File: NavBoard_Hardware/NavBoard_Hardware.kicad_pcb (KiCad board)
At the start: 2 copper layers, 124.5 x 79.2 mm, 41 parts, among them J1 Conn_01x06_Male, U1 OKI-5V, U2 BHI160B, U3 ICM-20608-G, U4 OKI-3V3, U6 Raspberry_Pi

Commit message: CDR Changes 2
Ready to release, signatures to be added
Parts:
- added G***: LOGO, MRDT_Silkscreens:0_MRDT_Logo_60mm, B.Cu at (92.2, 79.0)
- moved J1 9.91 mm to (48.0, 87.4)
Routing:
- net M8Q-TX: track 101.4 -> 111.3 mm
- net M8Q-RX: track 94.3 -> 104.2 mm
- net I2C-SDA: track 108.3 -> 118.2 mm
- net I2C-SCL: track 107.1 -> 117.0 mm
- net +5V: track 108.1 -> 118.0 mm
- net GND: track 93.1 -> 84.8 mm, vias 11 -> 10
- net Net-(C12-Pad1): track 3.25 -> 4.16 mm
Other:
- board text added: "+"
- board text added: "-"
- board text added: "Navigation Board, Rev 1.1 Mars Rover Design Team Missouri S&T, 2022 Malacki Ehlers and Jorge Noriega"
- board text added: "RX"
- board text added: "SCL"
- board text added: "SDA"
- board text added: "TX"

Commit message: Signature
Added my signature on the board. Still needs one more.
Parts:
- added G***: LOGO, MRDT_Silkscreens:z_sig_Jorge_Noriega_34.3mmx15.1mm, F.Cu at (138.5, 104.0)

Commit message: Fixed Signature
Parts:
- removed the G*** at (138.5, 104.0)
- added G***: LOGO, Signature:z_sig_Jorge_Noriega_34.3mmx15.1mm, F.Cu at (145.8, 103.0)

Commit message: Added signature
Final updates, ready to order
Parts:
- removed the G*** at (145.8, 103.0)
- added G***: LOGO, Signatures:z_sig_Jorge_Noriega_34.3mmx15.1mm, F.Cu at (142.2, 57.4)
- added G***: LOGO, Signatures:z_sig_Malacki_Ehlers_15.3mmx4.7mm, F.Cu at (142.0, 74.9)

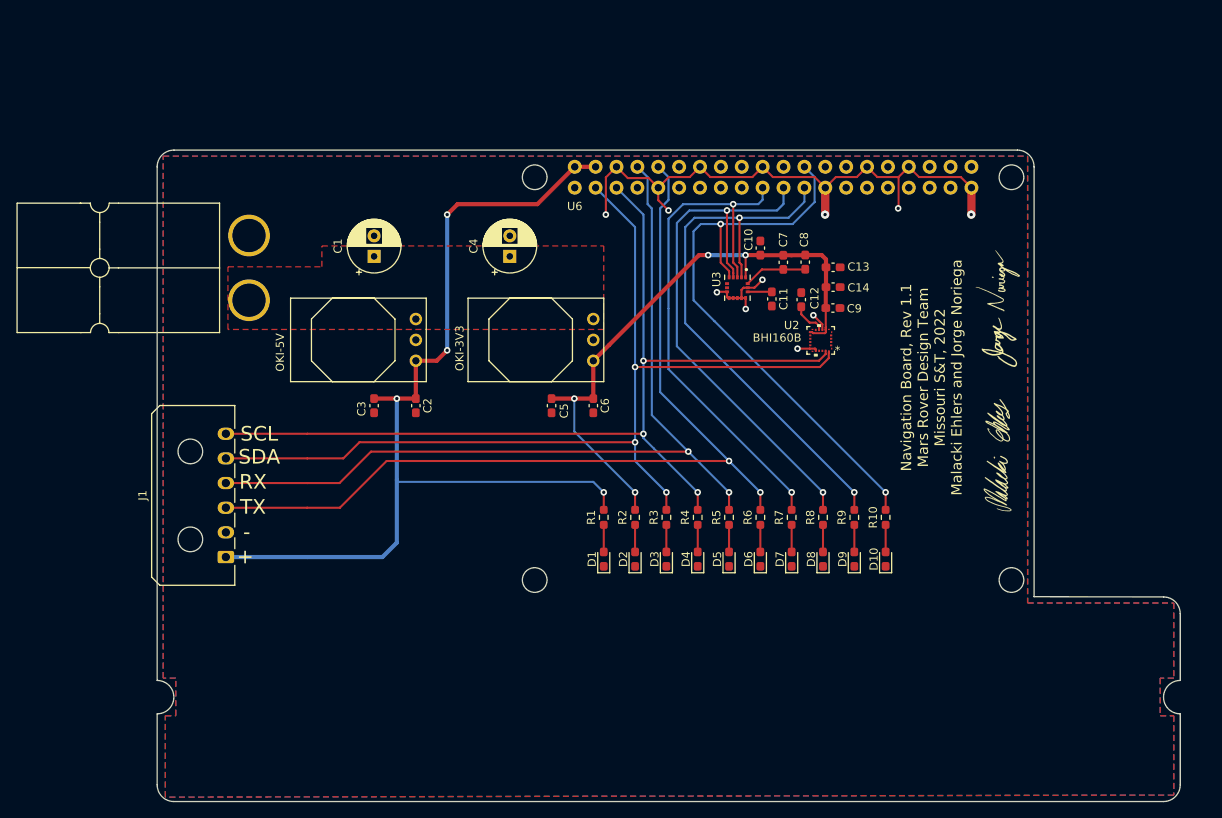
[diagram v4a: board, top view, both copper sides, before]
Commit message: Initial pass at stackable arrangement
Attempting to replace previous board design with 2 daughter boards, using a Teensy 4.1 instead of a Raspberry Pi
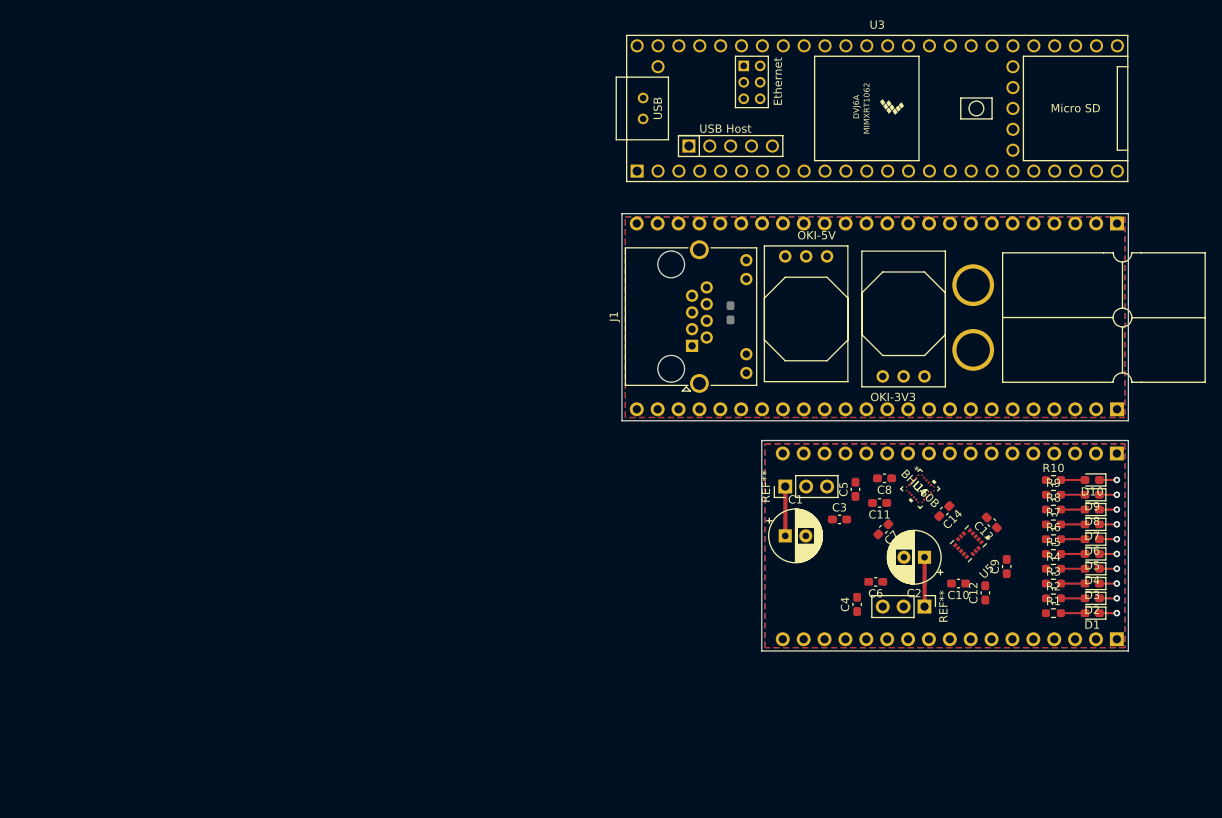
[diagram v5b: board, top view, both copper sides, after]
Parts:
- removed G***: LOGO, Signatures:z_sig_Jorge_Noriega_34.3mmx15.1mm
- removed G***: LOGO, Signatures:z_sig_Malacki_Ehlers_15.3mmx4.7mm
- removed G***: LOGO, MRDT_Silkscreens:0_MRDT_Logo_60mm
- removed U6: Raspberry_Pi, MRDT_Shields:RaspberryPi_THT_BOTTOM
- added C15: 0.1uF, Capacitor_SMD:C_0603_1608Metric_Pad1.08x0.95mm_HandSolder, B.Cu at (109.4, 57.7)
- added REF**: PinHeader_1x03_P2.54mm_Vertical, Connector_PinHeader_2.54mm:PinHeader_1x03_P2.54mm_Vertical, F.Cu at (133.0, 93.4)
- added REF**: PinHeader_1x03_P2.54mm_Vertical, Connector_PinHeader_2.54mm:PinHeader_1x03_P2.54mm_Vertical, F.Cu at (116.1, 78.8)
- added REF**: PinHeader_1x17_P2.54mm_Vertical, Connector_PinHeader_2.54mm:PinHeader_1x17_P2.54mm_Vertical, B.Cu at (156.4, 74.8)
- added REF**: PinSocket_1x24_P2.54mm_Vertical, Connector_PinSocket_2.54mm:PinSocket_1x24_P2.54mm_Vertical, B.Cu at (156.4, 69.4)
- added REF**: PinHeader_1x17_P2.54mm_Vertical, Connector_PinHeader_2.54mm:PinHeader_1x17_P2.54mm_Vertical, B.Cu at (156.4, 97.4)
- added REF**: PinSocket_1x24_P2.54mm_Vertical, Connector_PinSocket_2.54mm:PinSocket_1x24_P2.54mm_Vertical, B.Cu at (156.4, 46.8)
- added U5: ICM-20608-G, ICM-20608-G:ICM-20608-G, F.Cu at (138.3, 85.8)
- C10: value 10nF -> 0.47uF
- C12: value 0.47uF -> 2.2uF
- C13: value 1uF -> 10nF
- C2: value 10uF -> 22uF 50V; footprint Capacitor_SMD:C_0603_1608Metric_Pad1.08x0.95mm_HandSolder -> Capacitor_THT:CP_Radial_D6.3mm_P2.50mm
- C3: value 0.1uF -> 10uF
- C4: value 22uF 50V -> 10uF; footprint Capacitor_THT:CP_Radial_D6.3mm_P2.50mm -> Capacitor_SMD:C_0603_1608Metric_Pad1.08x0.95mm_HandSolder
- C5: value 10uF -> 0.1uF
- C7: value 0.1uF -> 1uF
- C8: value 2.2uF -> 0.1uF
- J1: value Conn_01x06_Male -> 8P8C_LED_Shielded; footprint Connector_Molex:Molex_Micro-Fit_3.0_43650-0600_1x06_P3.00mm_Horizontal -> Connector_RJ:RJ45_Amphenol_RJHSE538X
- U2: value BHI160B -> OKI-3V3; footprint BHI160B:BHI160B -> MRDT_Devices:OKI_Horizontal
- U3: value ICM-20608-G -> Teensy4.1; footprint ICM-20608-G:ICM-20608-G -> teensy:Teensy41
- U4: value OKI-3V3 -> BHI160B; footprint MRDT_Devices:OKI_Horizontal -> BHI160B:BHI160B
- moved Conn1 89.2 mm to (138.9, 62.2), turned to 180 degrees
- moved C2 64.6 mm to (133.0, 87.4), turned to 180 degrees
- moved J1 62.3 mm to (104.7, 61.7)
- moved C1 60.5 mm to (116.1, 84.8), turned to 0 degrees
- moved C4 59.8 mm to (124.8, 93.1)
- moved D1 59.8 mm to (153.4, 94.2), turned to 180 degrees
- moved C3 58.3 mm to (122.7, 82.8), turned to 0 degrees
- moved R1 55.9 mm to (148.7, 94.2), turned to 0 degrees
- moved D2 55.8 mm to (153.4, 92.4), turned to 180 degrees
- moved D3 51.9 mm to (153.4, 90.6), turned to 180 degrees
- moved R2 51.8 mm to (148.7, 92.4), turned to 0 degrees
- moved D4 48.0 mm to (153.4, 88.8), turned to 180 degrees
- moved R3 47.8 mm to (148.7, 90.6), turned to 0 degrees
- moved C10 47.4 mm to (137.1, 90.6), turned to 180 degrees
- moved U1 45.6 mm to (116.1, 50.8), turned to 0 degrees
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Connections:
- C10 pad 1: +3V3 -> Net-(C10-Pad1)
- C12 pad 1: Net-(C12-Pad1) -> +3V3
- C12 pad 2: GND -> Net-(C12-Pad2)
- C14 pad 1: +3V3 -> GND
- C14 pad 2: GND -> +3V3
- C2 pad 1: +5V -> +12V
- C4 pad 1: +12V -> +3V3
- C5 pad 1: +3V3 -> +5V
- C7 pad 2: Net-(C7-Pad2) -> GND
- C8 pad 2: Net-(C7-Pad2) -> GND
- C9 pad 1: GND -> +3V3
- C9 pad 2: +3V3 -> Net-(C12-Pad2)
- J1 pad 1: +5V -> /ETHERNET_TX+
- J1 pad 2: GND -> Net-(C15-Pad1)
- J1 pad 3: M8Q-TX -> /ETHERNET_TX-
- J1 pad 4: M8Q-RX -> /ETHERNET_RX+
- J1 pad 5: I2C-SDA -> Net-(C15-Pad1)
- J1 pad 6: I2C-SCL -> /ETHERNET_RX-
- R10 pad 1: ICM-CS -> unconnected-(R10-Pad1)
- R3 pad 1: I2C-SDA -> unconnected-(R3-Pad1)
- R4 pad 1: I2C-SCL -> unconnected-(R4-Pad1)
- R5 pad 1: M8Q-RX -> unconnected-(R5-Pad1)
- R6 pad 1: M8Q-TX -> unconnected-(R6-Pad1)
- R7 pad 1: ICM-SDI -> unconnected-(R7-Pad1)
- R8 pad 1: ICM-SDO -> unconnected-(R8-Pad1)
- R9 pad 1: ICM-SCLK -> unconnected-(R9-Pad1)
- U2 pad 1: Net-(U2-Pad1) -> +12V
- U2 pad 2: Net-(U2-Pad2) -> GND
- U2 pad 3: Net-(U2-Pad3) -> +3V3
- U3 pad 1: +3V3 -> GND
- U3 pad 10: GND -> unconnected-(U3-Pad10)
- U3 pad 11: GND -> unconnected-(U3-Pad11)
- U3 pad 12: GND -> unconnected-(U3-Pad12)
- U3 pad 13: GND -> /ICM_SDI
- U3 pad 14: Net-(C11-Pad1) -> /ICM_SDO
- U3 pad 15: GND -> unconnected-(U3-Pad15)
- U3 pad 16: Net-(C7-Pad2) -> unconnected-(U3-Pad16)
- U3 pad 2: ICM-SCLK -> unconnected-(U3-Pad2)
- U3 pad 3: ICM-SDI -> unconnected-(U3-Pad3)
- U3 pad 4: ICM-SDO -> unconnected-(U3-Pad4)
- U3 pad 5: ICM-CS -> unconnected-(U3-Pad5)
- U3 pad 6: Net-(U3-Pad6) -> unconnected-(U3-Pad6)
- U3 pad 7: (no net) -> unconnected-(U3-Pad7)
- U3 pad 8: GND -> unconnected-(U3-Pad8)
- U3 pad 9: GND -> unconnected-(U3-Pad9)
- U4 pad 1: +12V -> unconnected-(U4-Pad1)
- U4 pad 2: GND -> unconnected-(U4-Pad2)
- U4 pad 3: +3V3 -> unconnected-(U4-Pad3)
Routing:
- net I2C-SDA: track 118.2 -> 0.00 mm, vias 3 -> 0
- net +5V: track 118.0 -> 0.00 mm, vias 4 -> 0
- net I2C-SCL: track 117.0 -> 0.00 mm, vias 3 -> 0
- net M8Q-TX: track 111.3 -> 0.00 mm, vias 2 -> 0
- net M8Q-RX: track 104.2 -> 0.00 mm, vias 2 -> 0
- net +3V3: track 74.2 -> 0.00 mm, vias 4 -> 0
- net ICM-CS: track 71.5 -> 0.00 mm, vias 2 -> 0
- net ICM-SCLK: track 67.8 -> 0.00 mm, vias 2 -> 0
- net ICM-SDO: track 66.6 -> 0.00 mm, vias 2 -> 0
- net ICM-SDI: track 64.6 -> 0.00 mm, vias 2 -> 0
- net GND: track 84.8 -> 21.3 mm
- net +12V: track 0.00 -> 12.0 mm
- net Net-(C7-Pad2): track 7.68 -> 0.00 mm
- net Net-(C12-Pad1): track 4.16 -> 0.00 mm
- net Net-(C11-Pad1): track 2.93 -> 0.00 mm
- added copper zone on In1.Cu, net GND
- removed copper zone on F.Cu, net +12V
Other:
- board size 124.5 x 79.2 mm -> 61.6 x 53.2 mm
- copper layers 2 -> 4
- net class Default removed
- board text removed: "+"
- board text removed: "-"
- board text removed: "Navigation Board, Rev 1.1 Mars Rover Design Team Missouri S&T, 2022 Malacki Ehlers and Jorge Noriega"
- board text removed: "RX"
- board text removed: "SCL"
- board text removed: "SDA"
- board text removed: "TX"

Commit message: Redesigned layoput
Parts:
- removed D10, D6, D7, D8, D9: BLUE, LED_SMD:LED_0603_1608Metric_Pad1.05x0.95mm_HandSolder
- removed REF** (x2): PinHeader_1x03_P2.54mm_Vertical, Connector_PinHeader_2.54mm:PinHeader_1x03_P2.54mm_Vertical
- removed REF** (x2): PinHeader_1x17_P2.54mm_Vertical, Connector_PinHeader_2.54mm:PinHeader_1x17_P2.54mm_Vertical
- removed REF** (x2): PinSocket_1x24_P2.54mm_Vertical, Connector_PinSocket_2.54mm:PinSocket_1x24_P2.54mm_Vertical
- added J10: Conn_01x16, Connector_PinSocket_2.54mm:PinSocket_1x16_P2.54mm_Vertical, B.Cu at (197.2, 88.1)
- added J11: Conn_01x16, Connector_PinSocket_2.54mm:PinSocket_1x16_P2.54mm_Vertical, B.Cu at (197.2, 67.8)
- added J12: Conn_01x24, Connector_PinHeader_2.54mm:PinHeader_1x24_P2.54mm_Vertical, B.Cu at (138.8, 65.3)
- added J13: Conn_01x16, Connector_PinSocket_2.54mm:PinSocket_1x16_P2.54mm_Vertical, B.Cu at (263.8, 88.2)
- added J14: Conn_01x16, Connector_PinSocket_2.54mm:PinSocket_1x16_P2.54mm_Vertical, B.Cu at (263.8, 67.9)
- added J15: Conn_01x03, Connector_PinSocket_2.54mm:PinSocket_1x03_P2.54mm_Vertical, B.Cu at (230.7, 85.1)
- added J16: Conn_01x03, Connector_PinSocket_2.54mm:PinSocket_1x03_P2.54mm_Vertical, B.Cu at (236.3, 71.1)
- added J2: 6 Pin Molex Micro-Fit, Connector_Molex:Molex_Micro-Fit_3.0_43650-0600_1x06_P3.00mm_Horizontal, F.Cu at (222.1, 85.6)
- added J3: Conn_01x24, Connector_PinSocket_2.54mm:PinSocket_1x24_P2.54mm_Vertical, F.Cu at (56.7, 90.7)
- added J4: Conn_01x24, Connector_PinSocket_2.54mm:PinSocket_1x24_P2.54mm_Vertical, B.Cu at (56.7, 85.7)
- added J6: Conn_01x24, Connector_PinSocket_2.54mm:PinSocket_1x24_P2.54mm_Vertical, B.Cu at (56.7, 70.4)
- added J7: Conn_01x24, Connector_PinSocket_2.54mm:PinSocket_1x24_P2.54mm_Vertical, F.Cu at (56.7, 65.3)
- added J8: Conn_01x06, Connector_PinSocket_2.00mm:PinSocket_2x03_P2.00mm_Vertical, B.Cu at (153.8, 76.8)
- added J9: Conn_01x24, Connector_PinHeader_2.54mm:PinHeader_1x24_P2.54mm_Vertical, B.Cu at (197.3, 90.7)
- added JP1: Solder Jumper, Jumper:SolderJumper-2_P1.3mm_Open_RoundedPad1.0x1.5mm, F.Cu at (245.6, 101.1)
- added R11: 4.7k, Resistor_SMD:R_0603_1608Metric_Pad0.98x0.95mm_HandSolder, F.Cu at (207.7, 95.7)
- added R12: 100, Resistor_SMD:R_0603_1608Metric_Pad0.98x0.95mm_HandSolder, F.Cu at (193.1, 44.3)
- added R13: 100, Resistor_SMD:R_0603_1608Metric_Pad0.98x0.95mm_HandSolder, F.Cu at (59.2, 52.2)
- added R14: 100, Resistor_SMD:R_0603_1608Metric_Pad0.98x0.95mm_HandSolder, F.Cu at (63.6, 52.2)
- added TP1: TestPoint, TestPoint:TestPoint_Pad_D2.0mm, F.Cu at (187.2, 36.4)
- added TP2: TestPoint, TestPoint:TestPoint_Pad_D2.0mm, F.Cu at (192.5, 31.4)
- added TP3: TestPoint, TestPoint:TestPoint_Pad_D2.0mm, F.Cu at (206.7, 103.5)
- added TP4: TestPoint, TestPoint:TestPoint_Pad_D2.0mm, F.Cu at (211.0, 99.0)
- C1: value 22uF 50V -> 0.1uF; footprint Capacitor_THT:CP_Radial_D6.3mm_P2.50mm -> Capacitor_SMD:C_0603_1608Metric_Pad1.08x0.95mm_HandSolder
- C10: value 0.47uF -> 10uF
- C11: value 0.47uF -> 0.1uF
- C13: value 10nF -> 0.1uF
- C14: value 0.1uF -> 0.47uF
- C15: value 0.1uF -> 10nF; moved to F.Cu
- C2: value 22uF 50V -> 1uF; footprint Capacitor_THT:CP_Radial_D6.3mm_P2.50mm -> Capacitor_SMD:C_0603_1608Metric_Pad1.08x0.95mm_HandSolder
- C3, C4: value 10uF -> 0.1uF
- C5: value 0.1uF -> 0.47uF; footprint Capacitor_SMD:C_0603_1608Metric_Pad1.08x0.95mm_HandSolder -> Capacitor_THT:CP_Radial_D6.3mm_P2.50mm
- C6, C9: value 0.1uF -> 22uF 50V
- C7: value 1uF -> 10uF
- C8: footprint Capacitor_SMD:C_0603_1608Metric_Pad1.08x0.95mm_HandSolder -> Capacitor_THT:CP_Radial_D6.3mm_P2.50mm
- R1: value 100 -> 43
- R10, R3, R4, R5, R6, R7, R8, R9: value 100 -> 4.7k
- R2: value 43 -> 100
- U1: value OKI-5V -> BHI160B; footprint MRDT_Devices:OKI_Horizontal -> BHI160B:BHI160B
- U2: value OKI-3V3 -> OKI-5V
- U3: value Teensy4.1 -> OKI-3V3; footprint teensy:Teensy41 -> MRDT_Devices:OKI_Horizontal
- U4: value BHI160B -> ICM-20608-G; footprint BHI160B:BHI160B -> ICM-20608-G:ICM-20608-G
- U5: value ICM-20608-G -> Teensy4.1; footprint ICM-20608-G:ICM-20608-G -> teensy:Teensy41
- moved C15 161.2 mm to (260.0, 115.2), turned to 0 degrees
- moved C6 141.5 mm to (255.3, 30.6), turned to 0 degrees
- moved C5 136.1 mm to (260.5, 72.3), turned to -90 degrees
- moved C8 132.4 mm to (260.5, 81.4), turned to -90 degrees
- moved C9 128.2 mm to (268.0, 60.0), turned to 0 degrees
- moved C7 119.3 mm to (244.0, 56.1), turned to 0 degrees
- moved R4 118.3 mm to (264.4, 113.5)
- moved U1 117.6 mm to (231.0, 75.8)
- moved D2 108.5 mm to (260.0, 112.6), turned to 0 degrees
- moved R2 105.7 mm to (249.4, 124.5)
- moved U4 105.7 mm to (238.1, 79.6), turned to 0 degrees
- moved R3 102.2 mm to (245.0, 124.5)
- moved D4 101.9 mm to (59.3, 49.6), turned to 0 degrees
- moved D5 97.2 mm to (63.7, 49.6), turned to 0 degrees
- moved R1 96.9 mm to (240.7, 124.5)
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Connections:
- C1 pad 1: +12V -> Net-(C1-Pad1)
- C1 pad 2: GND -> Net-(C1-Pad2)
- C10 pad 1: Net-(C10-Pad1) -> +3V3
- C11 pad 1: Net-(C11-Pad1) -> +3V3
- C12 pad 2: Net-(C12-Pad2) -> GND
- C14 pad 1: GND -> +3V3
- C14 pad 2: +3V3 -> GND
- C15 pad 1: Net-(C15-Pad1) -> +3V3
- C15 pad 2: Net-(C15-Pad2) -> GND
- C2 pad 1: +12V -> +3V3
- C3 pad 1: +5V -> +3V3
- C5 pad 1: +5V -> +3V3
- C6 pad 1: +3V3 -> /OKI - 3V3/+12V
- C7 pad 1: +3V3 -> +5V
- C8 pad 1: +3V3 -> +5V
- C9 pad 1: +3V3 -> /OKI - 3V3/+12V
- C9 pad 2: Net-(C12-Pad2) -> GND
- Conn1 pad 2: +12V -> /OKI - 3V3/+12V
- D3 pad 1: GND -> /teensy_4.1/UART_Status_LED
- D4 pad 1: GND -> /teensy_4.1/SPI_Status_LED
- D5 pad 1: GND -> /teensy_4.1/I2C_Status_LED
- J1 pad 1: /ETHERNET_TX+ -> /Main Board/ETHERNET_TX+
- J1 pad 10: /ETHERNET_LED -> /Main Board/ETHERNET_LED
- J1 pad 2: Net-(C15-Pad1) -> Net-(C1-Pad1)
- J1 pad 3: /ETHERNET_TX- -> /Main Board/ETHERNET_TX-
- J1 pad 4: /ETHERNET_RX+ -> /Main Board/ETHERNET_RX+
- J1 pad 5: Net-(C15-Pad1) -> Net-(C1-Pad1)
- J1 pad 6: /ETHERNET_RX- -> /Main Board/ETHERNET_RX-
- J1 pad 8: Net-(C15-Pad2) -> Net-(C1-Pad2)
- R1 pad 1: +5V -> +3V3
- R10 pad 1: unconnected-(R10-Pad1) -> Net-(R10-Pad1)
- R10 pad 2: Net-(D10-Pad2) -> GND
- R2 pad 1: +3V3 -> +5V
- R3 pad 1: unconnected-(R3-Pad1) -> /I2C-SDA
- R3 pad 2: Net-(D3-Pad2) -> GND
- R4 pad 1: unconnected-(R4-Pad1) -> /I2C-SCL
- R4 pad 2: Net-(D4-Pad2) -> GND
- R5 pad 1: unconnected-(R5-Pad1) -> Net-(R5-Pad1)
- R5 pad 2: Net-(D5-Pad2) -> GND
- R6 pad 1: unconnected-(R6-Pad1) -> Net-(R6-Pad1)
- R6 pad 2: Net-(D6-Pad2) -> GND
- R7 pad 1: unconnected-(R7-Pad1) -> Net-(R7-Pad1)
- R7 pad 2: Net-(D7-Pad2) -> GND
- R8 pad 1: unconnected-(R8-Pad1) -> Net-(R8-Pad1)
- R8 pad 2: Net-(D8-Pad2) -> GND
- R9 pad 1: unconnected-(R9-Pad1) -> Net-(R9-Pad1)
- R9 pad 2: Net-(D9-Pad2) -> GND
- U1 pad 1: +12V -> (no net)
- U1 pad 2: GND -> (no net)
- U1 pad 3: +5V -> Net-(R8-Pad1)
- U2 pad 1: +12V -> /OKI - 3V3/+12V
- U2 pad 3: +3V3 -> +5V
- U3 pad 1: GND -> /OKI - 3V3/+12V
- U3 pad 2: unconnected-(U3-Pad2) -> GND
- U3 pad 3: unconnected-(U3-Pad3) -> +3V3
- U4 pad 1: unconnected-(U4-Pad1) -> +3V3
- U4 pad 10: Net-(C11-Pad1) -> unconnected-(U4-Pad10)
- U4 pad 13: +3V3 -> GND
- U4 pad 14: unconnected-(U4-Pad14) -> +3V3
- U4 pad 15: unconnected-(U4-Pad15) -> GND
- U4 pad 16: unconnected-(U4-Pad16) -> +3V3
- U4 pad 2: unconnected-(U4-Pad2) -> /SPI-SCLK
- U4 pad 3: unconnected-(U4-Pad3) -> /SPI-MOSI
- U4 pad 4: unconnected-(U4-Pad4) -> /SPI-MISO
- U4 pad 5: unconnected-(U4-Pad5) -> /SPI-CS
- U4 pad 6: unconnected-(U4-Pad6) -> Net-(R11-Pad1)
- U4 pad 7: unconnected-(U4-Pad7) -> (no net)
- U4 pad 8: +3V3 -> Net-(R10-Pad1)
- U4 pad 9: GND -> unconnected-(U4-Pad9)
- U5 pad 1: +3V3 -> GND
- U5 pad 10: GND -> /Teensy Shield/Pin8
- U5 pad 11: GND -> /Teensy Shield/Pin9
- U5 pad 12: GND -> /Teensy Shield/Pin10
- U5 pad 13: GND -> /Teensy Shield/Pin11
- U5 pad 14: Net-(C10-Pad1) -> /Teensy Shield/Pin12
- U5 pad 15: GND -> +3V3
- U5 pad 16: Net-(C12-Pad2) -> /Teensy Shield/Pin24
- U5 pad 2: /ICM_SCL -> /Teensy Shield/Pin0
- U5 pad 3: /ICM_SDI -> /Teensy Shield/Pin1
- U5 pad 4: /ICM_SDO -> /Teensy Shield/Pin2
- U5 pad 5: unconnected-(U5-Pad5) -> /Teensy Shield/Pin3
- U5 pad 6: unconnected-(U5-Pad6) -> /Teensy Shield/Pin4
- U5 pad 7: (no net) -> /Teensy Shield/Pin5
- U5 pad 8: GND -> /Teensy Shield/Pin6
- U5 pad 9: GND -> /Teensy Shield/Pin7
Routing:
- net +12V: track 12.0 -> 0.00 mm
- net GND: track 21.3 -> 15.2 mm, vias 10 -> 0
- net /Teensy Shield/Pin41: track 0.00 -> 5.08 mm
- net /Teensy Shield/Pin38: track 0.00 -> 5.08 mm
- net /Teensy Shield/Pin36: track 0.00 -> 5.08 mm
- net /Teensy Shield/Pin22: track 0.00 -> 5.08 mm
- net /Teensy Shield/Pin20: track 0.00 -> 5.08 mm
- net /Teensy Shield/Pin40: track 0.00 -> 5.08 mm
- net /Teensy Shield/Pin34: track 0.00 -> 5.08 mm
- net /Teensy Shield/Pin17: track 0.00 -> 5.08 mm
- net /Teensy Shield/Pin15: track 0.00 -> 5.08 mm
- net /Teensy Shield/Pin13: track 0.00 -> 5.08 mm
- net /Teensy Shield/Pin3V3_Right: track 0.00 -> 5.08 mm
- net +5V: track 0.00 -> 5.08 mm
- net /Teensy Shield/Pin39: track 0.00 -> 5.08 mm
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- removed copper zone on B.Cu, net GND
- removed copper zone on F.Cu, net GND
- removed copper zone on In1.Cu, net GND
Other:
- board size 61.6 x 53.2 mm -> 210.7 x 29 mm

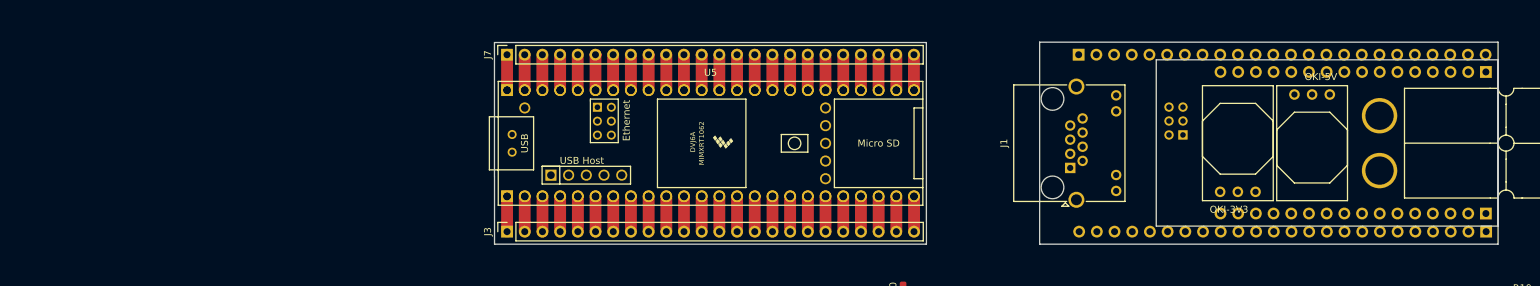
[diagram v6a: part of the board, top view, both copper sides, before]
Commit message: Created adapter symbols and footprints
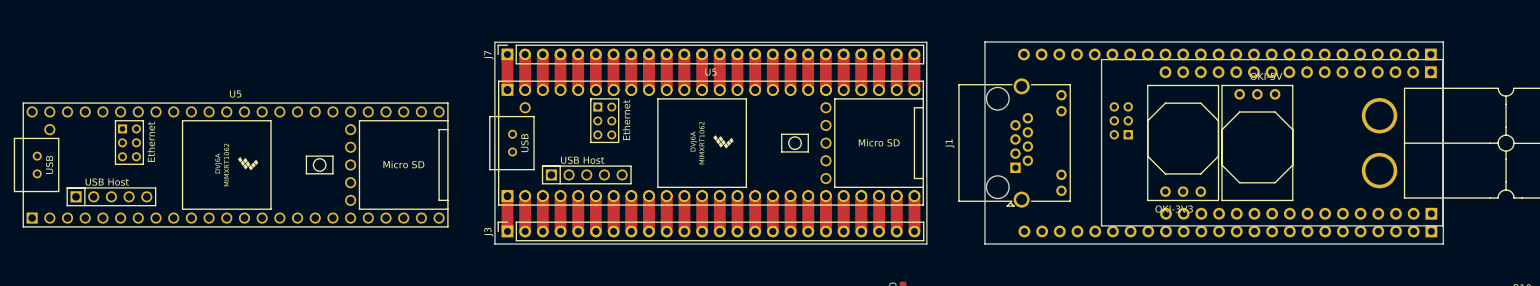
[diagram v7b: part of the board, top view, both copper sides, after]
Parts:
- added U5: Teensy4.1, teensy:Teensy41, F.Cu at (17.8, 81.2)
- moved J12 50.6 mm to (189.3, 65.3), turned to 90 degrees
- moved J11 7.90 mm to (189.3, 67.8)
- moved J1 7.86 mm to (129.7, 81.6)
- moved J8 7.86 mm to (145.9, 76.8)
- moved J9 7.86 mm to (189.4, 90.7)
- moved U2 7.86 mm to (161.9, 71.0)
- moved U3 7.86 mm to (156.3, 85.0)
- moved J10 7.83 mm to (189.4, 88.2)
- moved J3 0.07 mm to (56.8, 90.7)
- moved J4 0.07 mm to (56.8, 85.6)
- moved J6 0.07 mm to (56.8, 70.4)
- moved J7 0.07 mm to (56.8, 65.3)
- moved U5 0.07 mm to (86.0, 78.0)
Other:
- board size 210.7 x 29 mm -> 210.6 x 29 mm
